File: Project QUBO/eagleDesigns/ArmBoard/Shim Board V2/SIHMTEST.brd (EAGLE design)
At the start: 71.1 x 81.3 mm, 30 parts, among them IC1 MCP2551/SN, U1 BME280

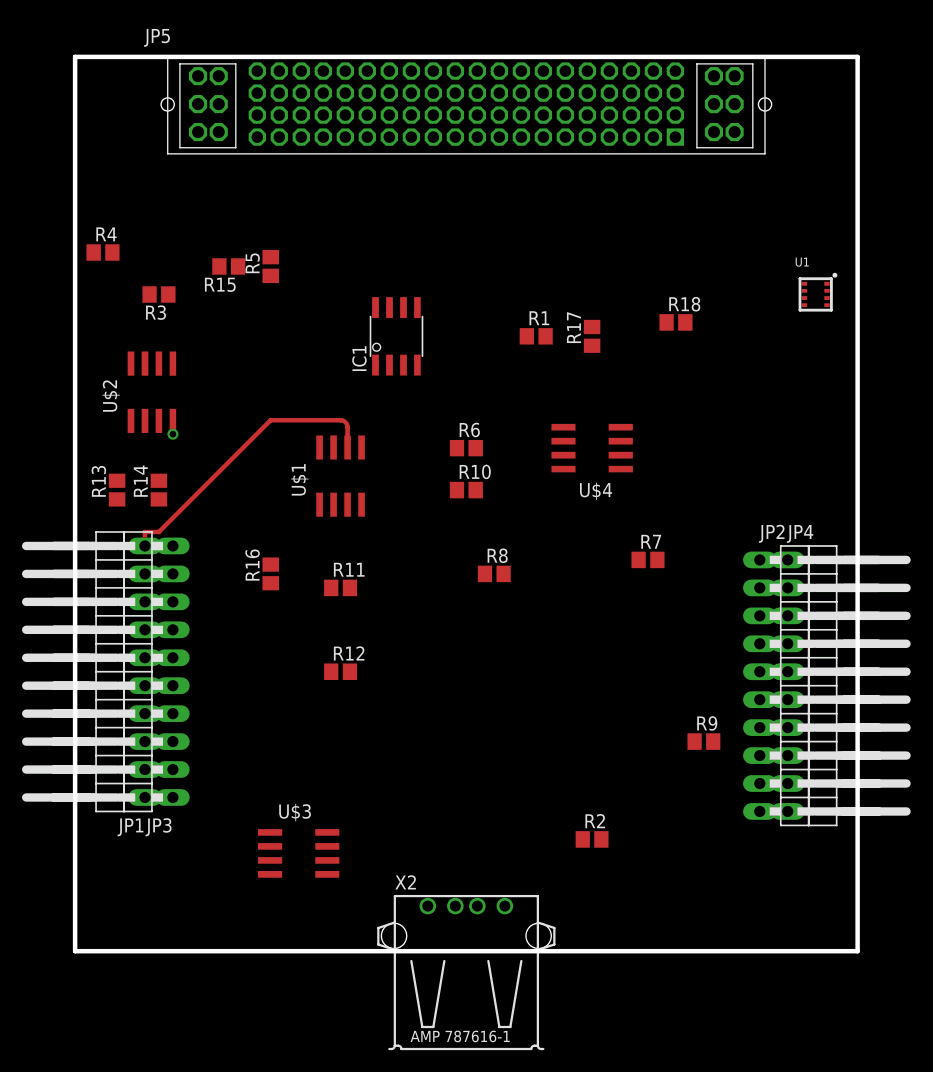
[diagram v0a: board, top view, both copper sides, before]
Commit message: 
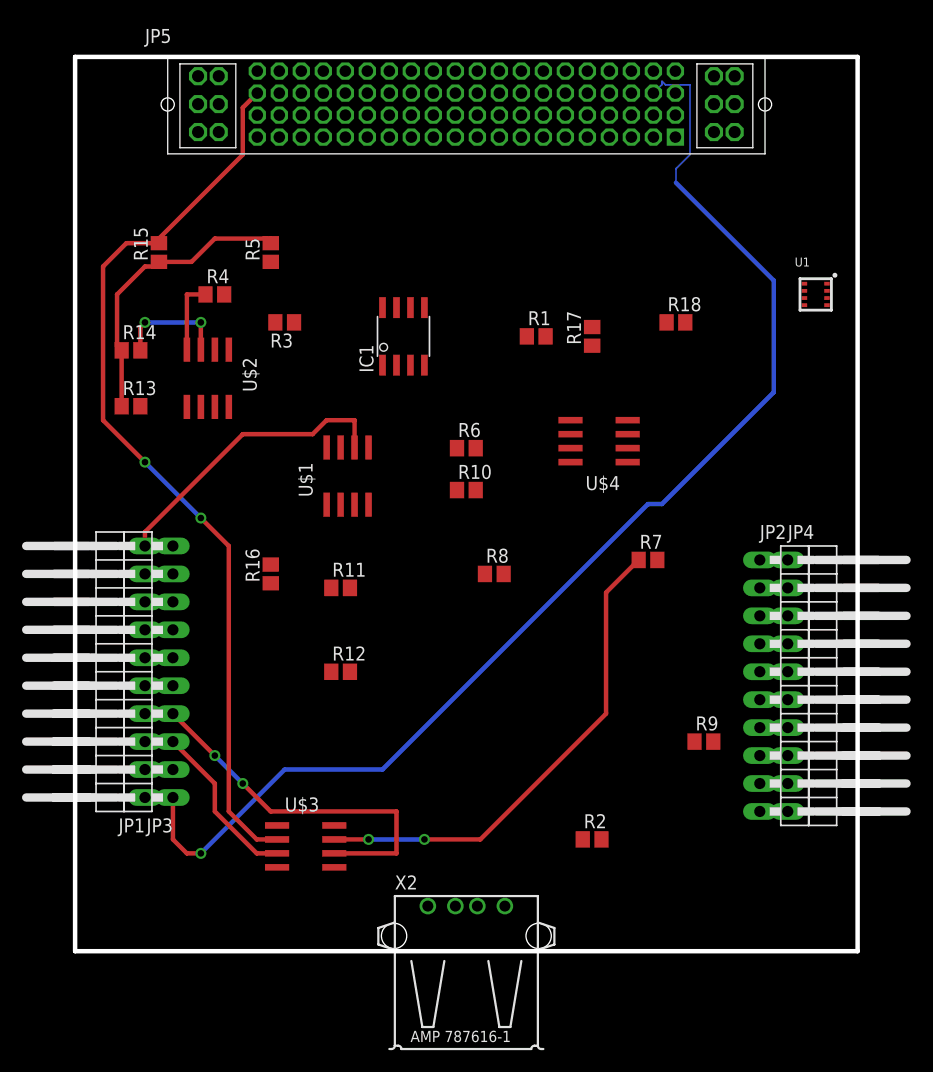
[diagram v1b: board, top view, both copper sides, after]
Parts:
- moved R14 13.0 mm to (5.08, 54.6), turned to 0 degrees
- moved R3 11.7 mm to (19.1, 57.1)
- moved R4 10.9 mm to (12.7, 59.7)
- moved R13 7.73 mm to (5.08, 49.5), turned to 0 degrees
- moved R15 6.48 mm to (7.62, 63.5), turned to 90 degrees
- moved U$2 5.24 mm to (12.1, 52.1), turned to 180 degrees
- moved R5 1.27 mm to (17.8, 63.5)
- moved U$3 0.90 mm to (21.0, 9.53)
- moved U$4 0.90 mm to (47.6, 46.4)
- moved U$1 0.64 mm to (24.8, 43.2)
- moved IC1 0.63 mm to (29.8, 55.9)
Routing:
- net 5.0(3): track 0.00 -> 112.5 mm, vias 0 -> 1
- net BUFFERSCL2: track 0.00 -> 83.0 mm, vias 0 -> 2
- net BUFFERSDA2: track 0.00 -> 44.6 mm, vias 0 -> 2
- net UNBUFFERSDA2: track 0.00 -> 33.5 mm, vias 0 -> 2
- net 5.0(BME): track 0.00 -> 27.2 mm
- net UNBUFFERSCL2: track 0.00 -> 15.2 mm
- net UNBUFFERSCL1: track 0.00 -> 10.3 mm, vias 0 -> 2
- net GND: track 0.00 -> 6.71 mm
- net UNBUFFERSDA0: track 26.0 -> 27.0 mm
- removed copper zone on layer 16, net N$3
- removed copper zone on layer 16, net N$4

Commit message: 
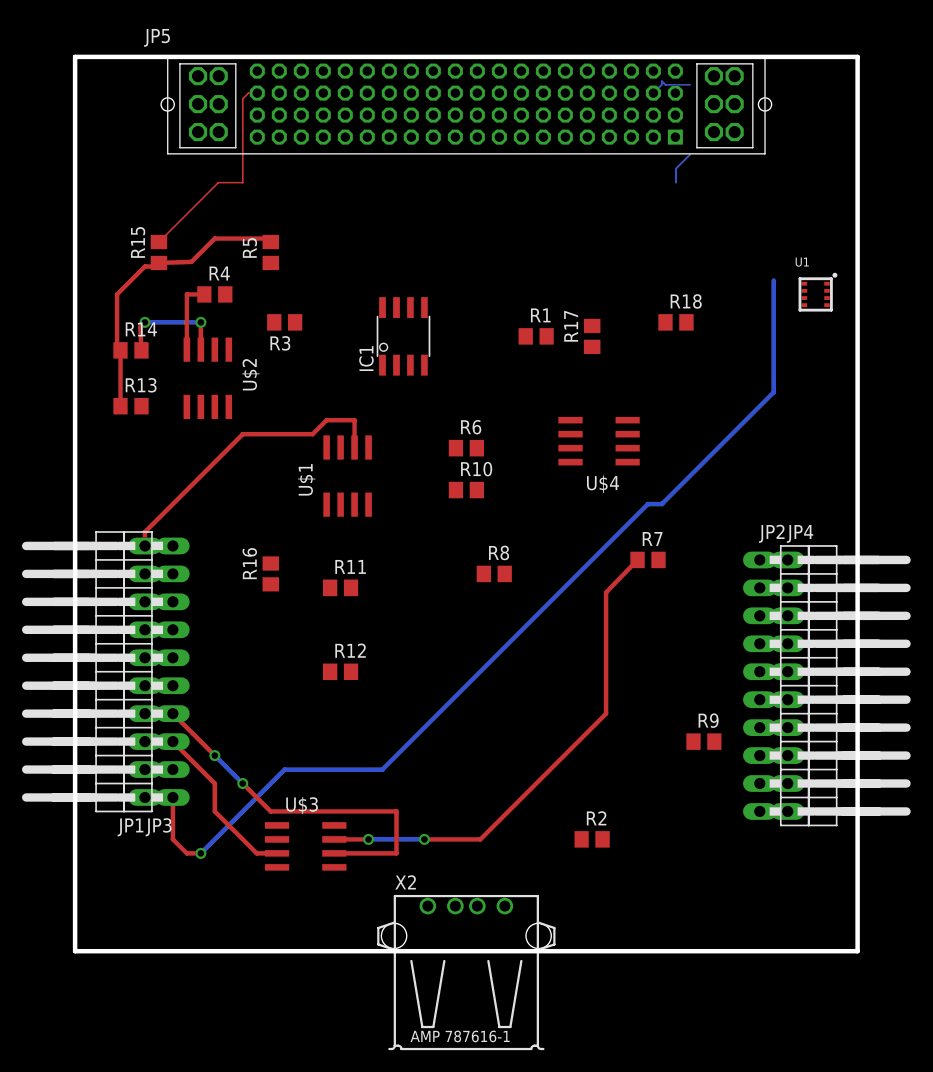
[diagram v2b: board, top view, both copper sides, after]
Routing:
- net BUFFERSCL2: track 83.0 -> 19.0 mm, vias 2 -> 0
- net 5.0(3): track 112.5 -> 93.6 mm

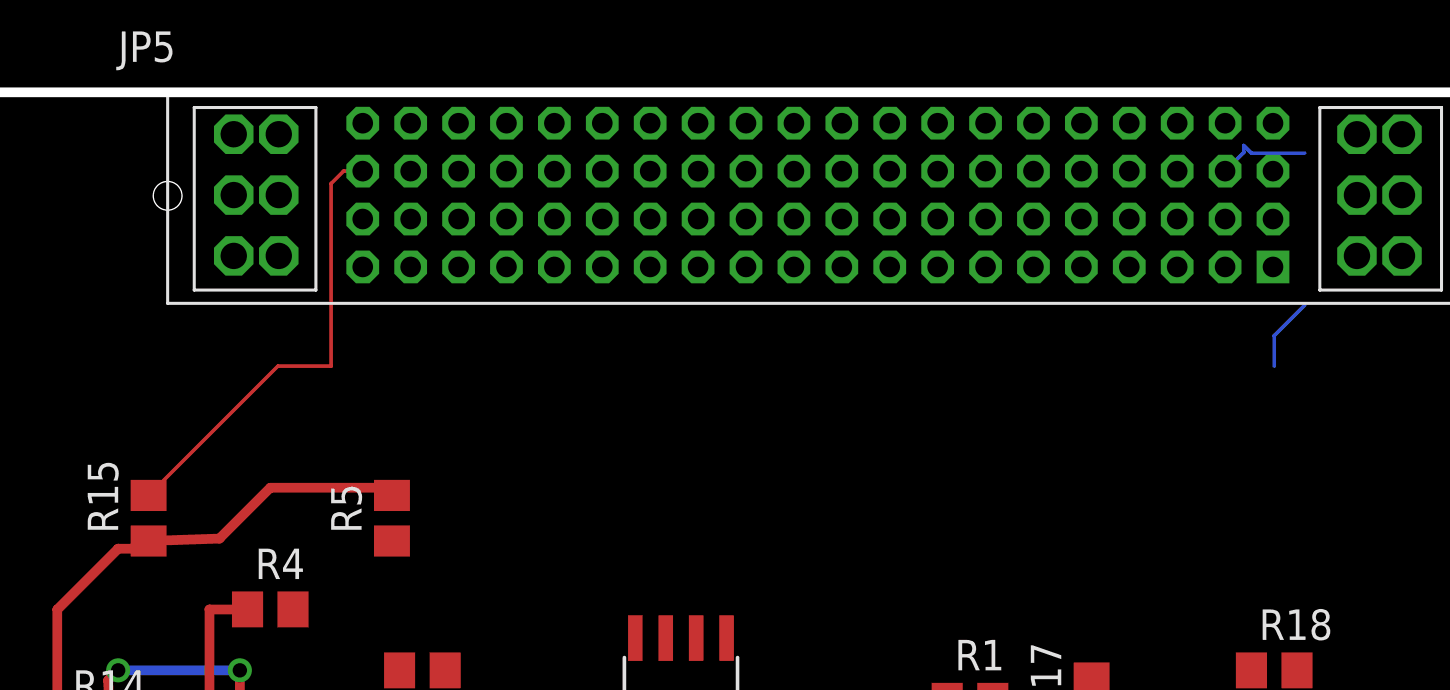
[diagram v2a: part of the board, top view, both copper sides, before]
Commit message: 
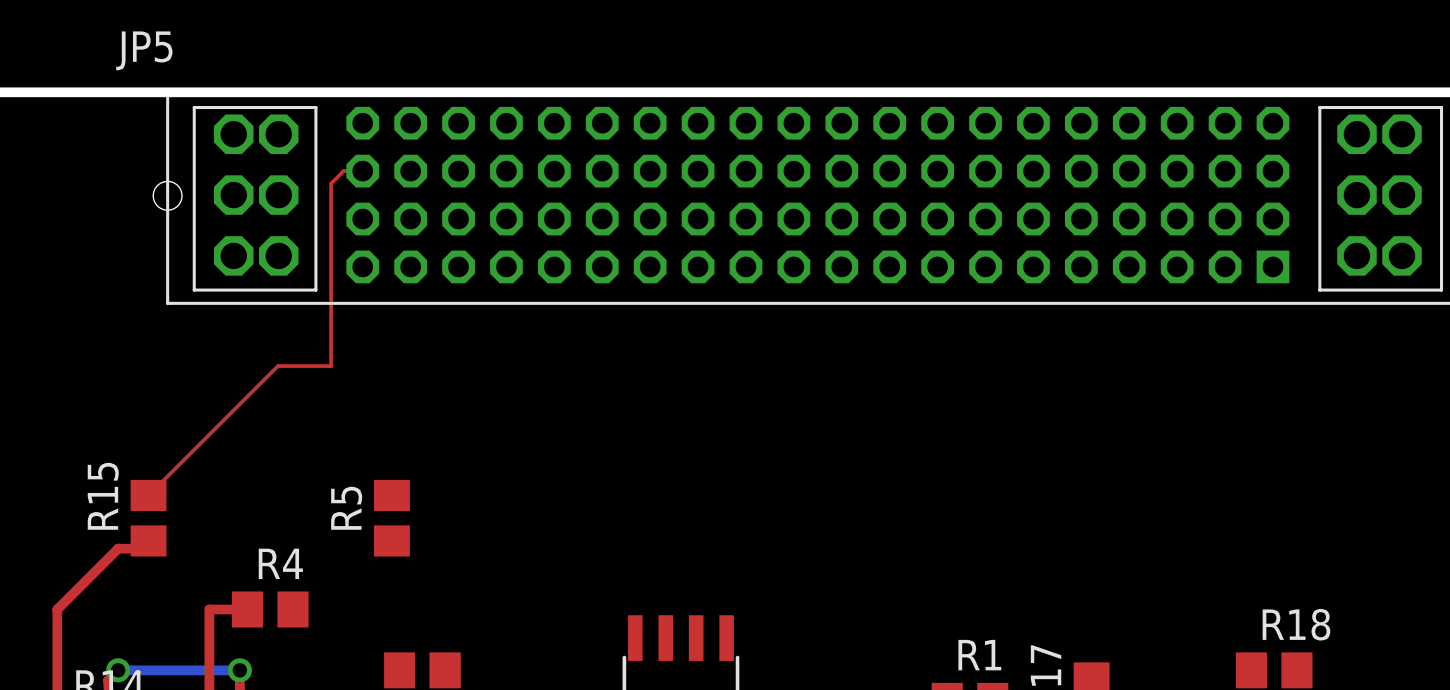
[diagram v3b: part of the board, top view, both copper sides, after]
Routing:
- net 5.0(BME): track 26.9 -> 16.3 mm
- net 5.0(3): track 93.6 -> 86.5 mm
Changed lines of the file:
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@@
 <wire x1="3.81" y1="59.69" x2="3.81" y2="55.03" width="0.4064" layer="1"/>
 <wire x1="3.81" y1="55.03" x2="4.13" y2="54.61" width="0.4064" layer="1"/>
+<wire x1="17.36" y1="64.77" x2="17.78" y2="64.45" width="0.4064" layer="1"/>
 <wire x1="53.66" y1="57.15" x2="68.335" y2="60.015" width="0" layer="19" extent="1-1"/>
 <wire x1="46.99" y1="54.93" x2="53.66" y2="57.15" width="0" layer="19" extent="1-1"/>
@@
 <wire x1="32.0599" y1="4.1001" x2="47.94" y2="10.16" width="0" layer="19" extent="1-1"/>
 <wire x1="4.13" y1="49.53" x2="17.78" y2="33.34" width="0" layer="19" extent="1-1"/>
-<wire x1="7.62" y1="62.55" x2="10.58" y2="62.65" width="0.4064" layer="1"/>
-<wire x1="10.58" y1="62.65" x2="12.7" y2="64.77" width="0.4064" layer="1"/>
-<wire x1="12.7" y1="64.77" x2="17.36" y2="64.77" width="0.4064" layer="1"/>
-<wire x1="17.36" y1="64.77" x2="17.78" y2="64.45" width="0.4064" layer="1"/>
+<wire x1="17.36" y1="64.77" x2="7.62" y2="62.55" width="0" layer="19" extent="1-1"/>
 </signal>
 <signal name="RES">
@@
 <wire x1="53.34" y1="40.64" x2="63.5" y2="50.8" width="0.4064" layer="16"/>
 <wire x1="63.5" y1="50.8" x2="63.5" y2="60.96" width="0.4064" layer="16"/>
-<wire x1="63.5" y1="60.96" x2="54.61" y2="69.85" width="0" layer="19" extent="1-16"/>
-<wire x1="54.61" y1="69.85" x2="54.61" y2="71.12" width="0.1524" layer="16"/>
-<wire x1="54.61" y1="71.12" x2="55.88" y2="72.39" width="0.1524" layer="16"/>
-<wire x1="55.88" y1="72.39" x2="55.88" y2="78.74" width="0" layer="19" extent="1-16"/>
-<wire x1="55.88" y1="78.74" x2="53.6575" y2="78.74" width="0.1524" layer="16"/>
-<wire x1="53.6575" y1="78.74" x2="53.34" y2="79.0575" width="0.1524" layer="16"/>
-<wire x1="53.34" y1="79.0575" x2="53.34" y2="78.77" width="0.1524" layer="16"/>
-<wire x1="53.34" y1="78.77" x2="52.56" y2="77.99" width="0.1524" layer="16"/>
+<wire x1="63.5" y1="60.96" x2="52.56" y2="77.99" width="0" layer="19" extent="16-16"/>
 </signal>
 <signal name="PE2">

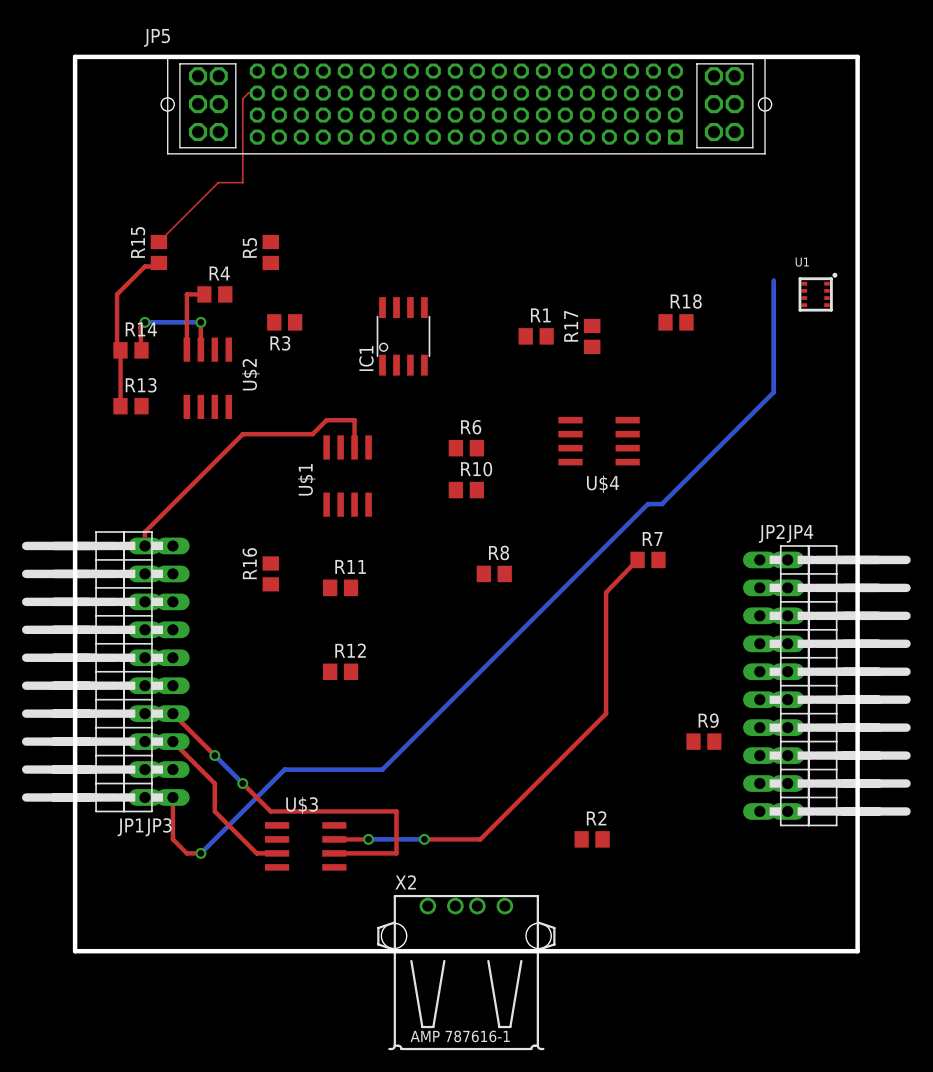
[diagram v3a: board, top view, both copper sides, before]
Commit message: 
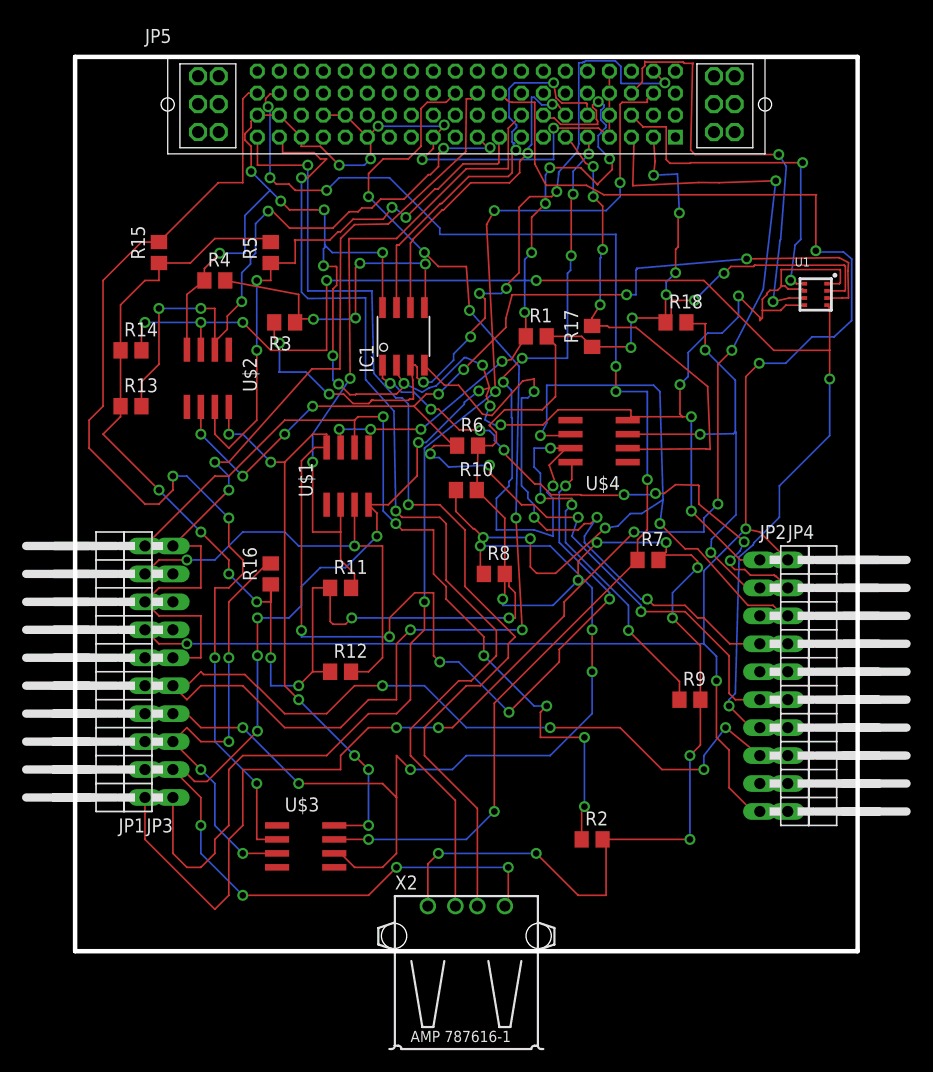
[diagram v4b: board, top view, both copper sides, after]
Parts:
- moved R9 4.02 mm to (55.9, 22.9)
- moved R4 1.27 mm to (12.7, 61.0)
- moved R6 0.26 mm to (35.7, 45.9)
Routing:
- net GND: track 6.61 -> 314.3 mm, vias 0 -> 32
- net 5.0(BME): track 16.3 -> 278.7 mm, vias 0 -> 26
- net MISO: track 0.00 -> 165.4 mm, vias 0 -> 10
- net SPI_CLK: track 0.00 -> 161.8 mm, vias 0 -> 5
- net BUFFERVCC: track 0.00 -> 131.1 mm, vias 0 -> 12
- net UNBUFFERSDA1: track 0.00 -> 130.9 mm, vias 0 -> 12
- net 3.3(1): track 0.00 -> 130.1 mm, vias 0 -> 6
- net UNBUFFERSCL1: track 10.3 -> 121.2 mm, vias 2 -> 7
- net USB+: track 0.00 -> 93.7 mm, vias 0 -> 2
- net USB-: track 0.00 -> 92.9 mm, vias 0 -> 2
- net BUFFERSDA3: track 0.00 -> 91.0 mm, vias 0 -> 10
- net MOSI: track 0.00 -> 81.7 mm, vias 0 -> 2
- net BUFFERSDA2: track 44.6 -> 120.4 mm, vias 2 -> 8
- net BUFFERSCL2: track 19.0 -> 94.4 mm, vias 0 -> 4
- net VDD: track 0.00 -> 73.2 mm, vias 0 -> 8
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
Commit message: 
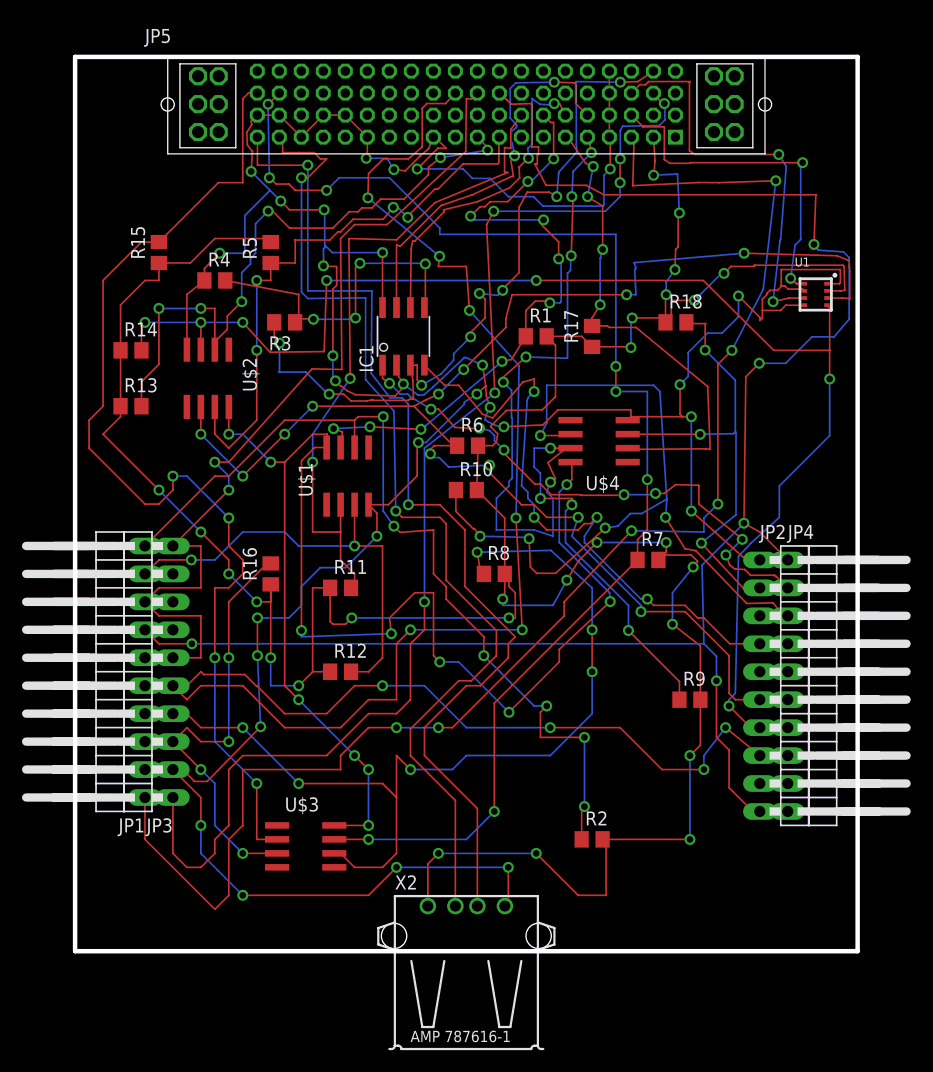
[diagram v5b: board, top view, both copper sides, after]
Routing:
- net VDD: track 73.2 -> 68.4 mm
- net 3.3(VDDIOBME): track 40.5 -> 36.8 mm
- net BUFFERSDA0: track 60.8 -> 58.4 mm
- net 5.0(3): track 109.5 -> 111.1 mm, vias 4 -> 6
- net GND: track 314.3 -> 315.4 mm, vias 32 -> 30
- net UNBUFFERSCL3: track 40.3 -> 41.4 mm
- net UNBUFFERSDA1: track 130.9 -> 131.8 mm
- net BUFFERSCL1: track 59.1 -> 58.2 mm
- net 5.0(BME): track 278.7 -> 277.9 mm
- net BUFFERSDA2: track 120.4 -> 119.7 mm
- net UNBUFFERSDA2: track 85.3 -> 84.8 mm
- net MISO: track 165.4 -> 165.9 mm
- net SPI_CLK: track 161.8 -> 162.4 mm
